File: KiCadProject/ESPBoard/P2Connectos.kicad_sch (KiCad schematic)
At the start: 0 parts

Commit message: ESP board layout mostly done. Small updates to battery management board
Signed-off-by: Eldalote.Electronics <Eldalote.Electronics@gmail.com>
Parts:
- added D201, D202, D203, D204, D205, D206, D207, D208, D209, D210, D211, D212, D213, D214, D215, D216, D217, D218, D219, D220: 3v3, Diode_SMD:D_0402_1005Metric, symbol Device:D_TVS
- added J201, J203: Conn_02x05, Connector_PinSocket_1.27mm:PinSocket_2x05_P1.27mm_Vertical_SMD, symbol Connector_Generic:Conn_02x05_Odd_Even
- added J202: Conn_01x02, Connector_PinSocket_1.27mm:PinSocket_1x02_P1.27mm_Vertical_SMD_Pin1Left, symbol Connector:Conn_01x02_Female
- added J204, J207: JST_SM04B, Connector_JST:JST_SH_SM04B-SRSS-TB_1x04-1MP_P1.00mm_Horizontal, symbol Connector:Conn_01x04_Male
- added J205: DNP, Connector_PinHeader_1.27mm:PinHeader_1x04_P1.27mm_Vertical, symbol Connector:Conn_01x04_Male
- added J206: JST_B5B_XH, Connector_JST:JST_XH_B5B-XH-A_1x05_P2.50mm_Vertical, symbol Connector:Conn_01x05_Male
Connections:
- new net +3V3: D205.2 (A2), D208.2 (A2), D217.2 (A2), D220.2 (A2), J201.1 (Pin_1), J201.2 (Pin_2), J203.1 (Pin_1), J203.2 (Pin_2), J205.1 (Pin_1), J207.1 (Pin_1)
- new net BQ_CHRG_OK: D203.2 (A2), J201.8 (Pin_8)
- new net BQ_CMPOUT: D211.2 (A2), J203.8 (Pin_8)
- new net BQ_EN_OTG: D212.2 (A2), J203.4 (Pin_4)
- new net BQ_IADPT: D210.2 (A2), J203.7 (Pin_7)
- new net BQ_IBAT: D209.2 (A2), J203.3 (Pin_3)
- new net C_USB_D+: D206.2 (A2), J202.1 (Pin_1)
- new net C_USB_D-: D207.2 (A2), J202.2 (Pin_2)
- new net Cell1: J206.4 (Pin_4)
- new net Cell2: J206.3 (Pin_3)
- new net Cell3: J206.2 (Pin_2)
- new net Cell4: J206.1 (Pin_1)
- new net GND: D201.1 (A1), D202.1 (A1), D203.1 (A1), D204.1 (A1), D205.1 (A1), D206.1 (A1), D207.1 (A1), D208.1 (A1), D209.1 (A1), D210.1 (A1), D211.1 (A1), D212.1 (A1), D213.1 (A1), D214.1 (A1), D215.1 (A1), D216.1 (A1), D217.1 (A1), D218.1 (A1), D219.1 (A1), D220.1 (A1), J201.10 (Pin_10), J201.5 (Pin_5), J201.6 (Pin_6), J201.9 (Pin_9), J203.10 (Pin_10), J203.5 (Pin_5), J203.6 (Pin_6), J203.9 (Pin_9), J204.1 (Pin_1), J204.4 (Pin_4), J205.4 (Pin_4), J206.5 (Pin_5), J207.4 (Pin_4)
- new net I2C_SCL: D204.2 (A2), D218.2 (A2), J201.4 (Pin_4), J207.3 (Pin_3)
- new net I2C_SDA: D201.2 (A2), D219.2 (A2), J201.3 (Pin_3), J207.2 (Pin_2)
- new net MAINLED_PWM: D213.2 (A2), J204.3 (Pin_3)
- new net MAINLED_nFTL: D214.2 (A2), J204.2 (Pin_2)
- new net UART_RXDO: D216.2 (A2), J205.2 (Pin_2)
- new net UART_TXDO: D215.2 (A2), J205.3 (Pin_3)
- new net USBPD_INT_N: D202.2 (A2), J201.7 (Pin_7)
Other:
- note added: "Back up programming pins"
- note added: "Battery Balancing port"
- note added: "Board to board "home made mezzanine" connection to Battery management PCB"
- note added: "Direct lines to LED driver board"
- note added: "I2C connector to hall board, daisy over to led driver board from there"

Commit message: Tweaking
Signed-off-by: Eldalote.Electronics <Eldalote.Electronics@gmail.com>
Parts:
- removed D201, D202, D203, D204, D205, D206, D207, D208, D209, D210, D211, D212, D213, D214, D215, D216, D217, D218, D219, D220: 3v3, Diode_SMD:D_0402_1005Metric, symbol Device:D_TVS
- J205: footprint Connector_PinHeader_1.27mm:PinHeader_1x04_P1.27mm_Vertical -> Connector_PinHeader_1.27mm:PinHeader_2x02_P1.27mm_Vertical_SMD
- J206: value JST_B5B_XH -> 1x05 female; footprint Connector_JST:JST_XH_B5B-XH-A_1x05_P2.50mm_Vertical -> Connector_PinSocket_1.27mm:PinSocket_1x05_P1.27mm_Vertical_SMD_Pin1Left; symbol Connector:Conn_01x05_Male -> Connector:Conn_01x05_Female

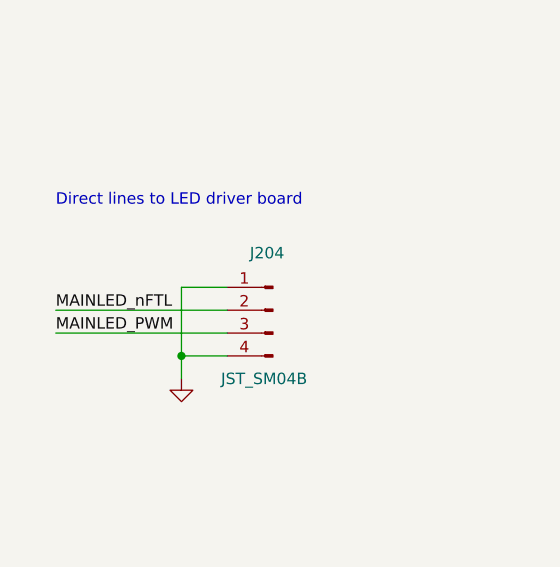
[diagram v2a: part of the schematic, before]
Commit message: Final touches before component order and PCB layout
Signed-off-by: Eldalote.Electronics <Eldalote.Electronics@gmail.com>
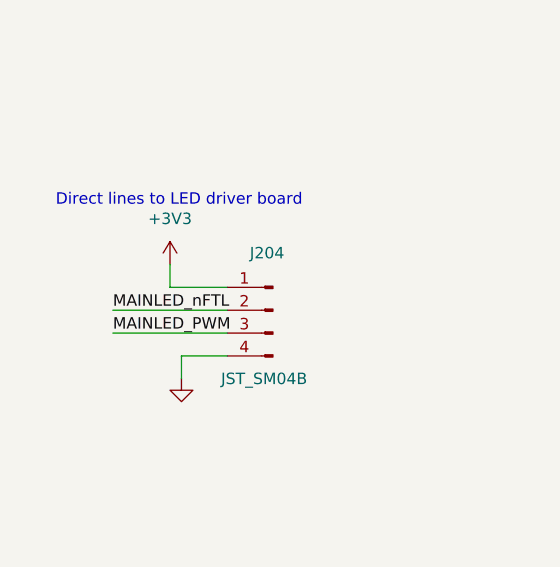
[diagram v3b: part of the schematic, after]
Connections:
- net +3V3: now also J204.1 (Pin_1)
- net GND: no longer J204.1 (Pin_1)
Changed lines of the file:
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@@
   (junction (at 95.25 69.85) (diameter 0) (color 0 0 0 0)
   )
-  (junction (at 36.83 154.94) (diameter 0) (color 0 0 0 0)
-  )
   (wire (pts (xy 142.24 171.45) (xy 154.94 171.45))
     (stroke (width 0) (type default) (color 0 0 0 0))
@@
     (stroke (width 0) (type default) (color 0 0 0 0))
   )
-  (wire (pts (xy 22.86 149.86) (xy 41.91 149.86))
+  (wire (pts (xy 29.21 149.86) (xy 41.91 149.86))
     (stroke (width 0) (type default) (color 0 0 0 0))
   )
@@
     (stroke (width 0) (type default) (color 0 0 0 0))
   )
-  (wire (pts (xy 36.83 147.32) (xy 36.83 154.94))
-    (stroke (width 0) (type default) (color 0 0 0 0))
-  )
   (wire (pts (xy 34.29 43.18) (xy 46.99 43.18))
     (stroke (width 0) (type default) (color 0 0 0 0))
@@
     (stroke (width 0) (type default) (color 0 0 0 0))
   )
-  (wire (pts (xy 41.91 147.32) (xy 36.83 147.32))
+  (wire (pts (xy 35.56 147.32) (xy 41.91 147.32))
     (stroke (width 0) (type default) (color 0 0 0 0))
   )
@@
     (stroke (width 0) (type default) (color 0 0 0 0))
   )
-  (wire (pts (xy 22.86 152.4) (xy 41.91 152.4))
+  (wire (pts (xy 29.21 152.4) (xy 41.91 152.4))
+    (stroke (width 0) (type default) (color 0 0 0 0))
+  )
+  (wire (pts (xy 35.56 147.32) (xy 35.56 144.78))
     (stroke (width 0) (type default) (color 0 0 0 0))
   )
@@
     (effects (font (size 1.27 1.27)) (justify left bottom))
   )
-  (label "MAINLED_PWM" (at 22.86 152.4 0)
+  (label "MAINLED_PWM" (at 29.21 152.4 0)
     (effects (font (size 1.27 1.27)) (justify left bottom))
   )
@@
     (effects (font (size 1.27 1.27)) (justify right bottom))
   )
-  (label "MAINLED_nFTL" (at 22.86 149.86 0)
+  (label "MAINLED_nFTL" (at 29.21 149.86 0)
     (effects (font (size 1.27 1.27)) (justify left bottom))
   )
@@
       (effects (font (size 1.27 1.27)) hide)
     )
+    (pin "1")
+  )
+  (symbol (lib_id "power:+3V3") (at 35.56 144.78 0) (unit 1)
+    (in_bom yes) (on_board yes)
+    (property "Reference" "#PWR?" (id 0) (at 35.56 148.59 0)
+      (effects (font (size 1.27 1.27)) hide)
+    )
+    (property "Value" "+3V3" (id 1) (at 35.56 139.7 0))
+    (property "Footprint" "" (id 2) (at 35.56 144.78 0)
+      (effects (font (size 1.27 1.27)) hide)
+    )
+    (property "Datasheet" "" (id 3) (at 35.56 144.78 0)
+      (effects (font (size 1.27 1.27)) hide)
+    )

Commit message: Components selected, MfID added to schematics, and components ordered
Signed-off-by: Eldalote.Electronics <Eldalote.Electronics@gmail.com>
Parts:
- J201, J203: MfID (none) -> 20021321-00010C4LF
- J202: MfID (none) -> M50-3140245
- J204, J207: MfID (none) -> SM04B-SRSS-TB(LF)(SN)
- J205: MfID (none) -> GRPB022VWQS-RC
- J206: MfID (none) -> M50-3140545
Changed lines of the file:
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@@
+      (effects (font (size 1.27 1.27)) hide)
+    )
+    (property "MfID" "M50-3140545" (id 4) (at 245.11 129.54 0)
       (effects (font (size 1.27 1.27)) hide)
     )
@@
   (symbol (lib_id "power:+3V3") (at 35.56 144.78 0) (unit 1)
     (in_bom yes) (on_board yes)
-    (property "Reference" "#PWR?" (id 0) (at 35.56 148.59 0)
+    (property "Reference" "#PWR0110" (id 0) (at 35.56 148.59 0)
       (effects (font (size 1.27 1.27)) hide)
     )
@@
       (effects (font (size 1.27 1.27)) hide)
     )
+    (property "MfID" "M50-3140245" (id 4) (at 255.27 46.99 0)
+      (effects (font (size 1.27 1.27)) hide)
+    )
     (pin "1")
     (pin "2")
@@
       (effects (font (size 1.27 1.27)) hide)
     )
+    (property "MfID" "GRPB022VWQS-RC" (id 4) (at 160.02 168.91 0)
+      (effects (font (size 1.27 1.27)) hide)
+    )
     (pin "1")
     (pin "2")
@@
       (effects (font (size 1.27 1.27)) hide)
     )
+    (property "MfID" "SM04B-SRSS-TB(LF)(SN)" (id 4) (at 125.73 110.49 0)
+      (effects (font (size 1.27 1.27)) hide)
+    )
     (pin "1")
     (pin "2")
@@
     )
     (property "Datasheet" "~" (id 3) (at 46.99 149.86 0)
+      (effects (font (size 1.27 1.27)) hide)
+    )
+    (property "MfID" "SM04B-SRSS-TB(LF)(SN)" (id 4) (at 46.99 149.86 0)
       (effects (font (size 1.27 1.27)) hide)
     )
@@
     )
     (property "Datasheet" "~" (id 3) (at 109.22 53.34 0)
+      (effects (font (size 1.27 1.27)) hide)
+    )
+    (property "MfID" "20021321-00010C4LF" (id 4) (at 109.22 53.34 0)
       (effects (font (size 1.27 1.27)) hide)
     )
@@
       (effects (font (size 1.27 1.27)) hide)
     )
+    (property "MfID" "20021321-00010C4LF" (id 4) (at 184.15 54.61 0)
+      (effects (font (size 1.27 1.27)) hide)
+    )

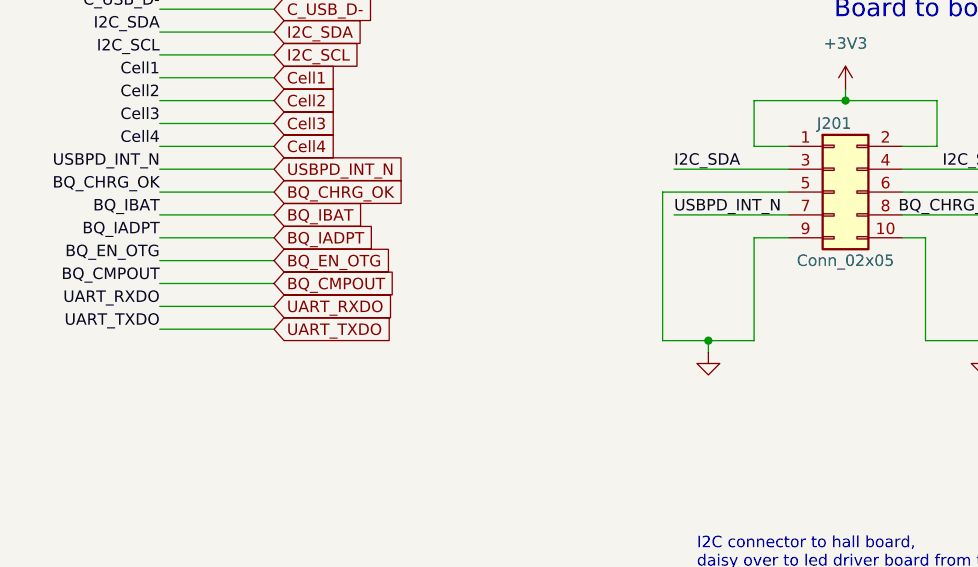
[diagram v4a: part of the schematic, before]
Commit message: Finished v0.1 of BatMan PCB, started layout of ESP PCB
Signed-off-by: Eldalote.Electronics <Eldalote.Electronics@gmail.com>
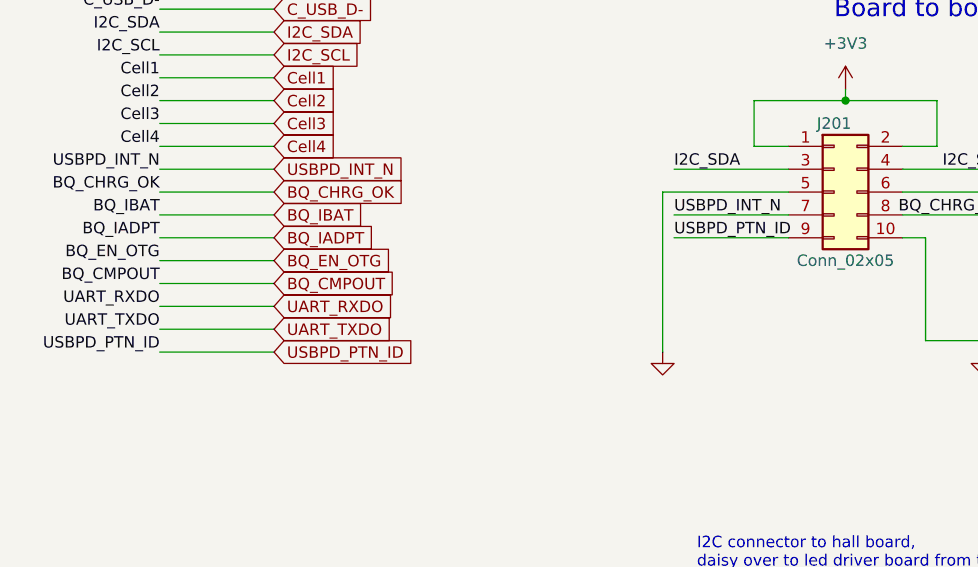
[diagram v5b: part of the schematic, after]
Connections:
- net GND: no longer J201.9 (Pin_9)
- new net USBPD_PTN_ID: J201.9 (Pin_9)
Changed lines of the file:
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@@
   (junction (at 172.72 68.58) (diameter 0) (color 0 0 0 0)
   )
-  (junction (at 95.25 69.85) (diameter 0) (color 0 0 0 0)
-  )
   (wire (pts (xy 142.24 171.45) (xy 154.94 171.45))
     (stroke (width 0) (type default) (color 0 0 0 0))
@@
     (stroke (width 0) (type default) (color 0 0 0 0))
   )
-  (wire (pts (xy 90.17 53.34) (xy 90.17 69.85))
+  (wire (pts (xy 90.17 53.34) (xy 90.17 71.12))
     (stroke (width 0) (type default) (color 0 0 0 0))
   )
@@
     (stroke (width 0) (type default) (color 0 0 0 0))
   )
-  (wire (pts (xy 95.25 69.85) (xy 100.33 69.85))
-    (stroke (width 0) (type default) (color 0 0 0 0))
-  )
   (wire (pts (xy 34.29 60.96) (xy 46.99 60.96))
     (stroke (width 0) (type default) (color 0 0 0 0))
@@
     (stroke (width 0) (type default) (color 0 0 0 0))
   )
+  (wire (pts (xy 91.44 58.42) (xy 104.14 58.42))
+    (stroke (width 0) (type default) (color 0 0 0 0))
+  )
   (wire (pts (xy 185.42 43.18) (xy 185.42 44.45))
     (stroke (width 0) (type default) (color 0 0 0 0))
   )
+  (wire (pts (xy 34.29 71.12) (xy 46.99 71.12))
+    (stroke (width 0) (type default) (color 0 0 0 0))
+  )
   (wire (pts (xy 234.95 134.62) (xy 234.95 137.16))
     (stroke (width 0) (type default) (color 0 0 0 0))
@@
     (stroke (width 0) (type default) (color 0 0 0 0))
   )
-  (wire (pts (xy 95.25 71.12) (xy 95.25 69.85))
-    (stroke (width 0) (type default) (color 0 0 0 0))
-  )
   (wire (pts (xy 195.58 44.45) (xy 195.58 49.53))
     (stroke (width 0) (type default) (color 0 0 0 0))
   )
-  (wire (pts (xy 100.33 58.42) (xy 100.33 69.85))
-    (stroke (width 0) (type default) (color 0 0 0 0))
-  )
   (wire (pts (xy 205.74 54.61) (xy 191.77 54.61))
     (stroke (width 0) (type default) (color 0 0 0 0))
@@
     (stroke (width 0) (type default) (color 0 0 0 0))
   )
-  (wire (pts (xy 90.17 69.85) (xy 95.25 69.85))
-    (stroke (width 0) (type default) (color 0 0 0 0))
-  )
   (wire (pts (xy 34.29 50.8) (xy 46.99 50.8))
     (stroke (width 0) (type default) (color 0 0 0 0))
@@
   )
   (wire (pts (xy 172.72 68.58) (xy 167.64 68.58))
-    (stroke (width 0) (type default) (color 0 0 0 0))
-  )
-  (wire (pts (xy 100.33 58.42) (xy 104.14 58.42))
     (stroke (width 0) (type default) (color 0 0 0 0))
   )
@@
     (effects (font (size 1.27 1.27)) (justify right bottom))
   )
+  (label "USBPD_PTN_ID" (at 34.29 71.12 180)
+    (effects (font (size 1.27 1.27)) (justify right bottom))
+  )
   (label "C_USB_D+" (at 233.68 46.99 0)
     (effects (font (size 1.27 1.27)) (justify left bottom))
@@
     (effects (font (size 1.27 1.27)) (justify left bottom))
   )
+  (label "USBPD_PTN_ID" (at 91.44 58.42 0)
+    (effects (font (size 1.27 1.27)) (justify left bottom))
+  )
   (label "BQ_IBAT" (at 171.45 52.07 0)
     (effects (font (size 1.27 1.27)) (justify left bottom))
@@
     (effects (font (size 1.27 1.27)) (justify left))
     (property "Intersheet References" "${INTERSHEET_REFS}" (id 0) (at 59.2607 30.4006 0)
+      (effects (font (size 1.27 1.27)) (justify left) hide)
+    )
+  )
+  (global_label "USBPD_PTN_ID" (shape input) (at 46.99 71.12 0) (fields_autoplaced)
+    (effects (font (size 1.27 1.27)) (justify left))
+    (property "Intersheet References" "${INTERSHEET_REFS}" (id 0) (at 63.1312 71.0406 0)
       (effects (font (size 1.27 1.27)) (justify left) hide)
     )
@@
     (pin "4")
   )
-  (symbol (lib_id "power:GND") (at 95.25 71.12 0) (unit 1)
+  (symbol (lib_id "power:GND") (at 90.17 71.12 0) (unit 1)
     (in_bom yes) (on_board yes) (fields_autoplaced)
-    (property "Reference" "#PWR0201" (id 0) (at 95.25 77.47 0)
-      (effects (font (size 1.27 1.27)) hide)
-    )
-    (property "Value" "GND" (id 1) (at 95.25 76.2 0)
-      (effects (font (size 1.27 1.27)) hide)
-    )
-    (property "Footprint" "" (id 2) (at 95.25 71.12 0)
-      (effects (font (size 1.27 1.27)) hide)
-    )
-    (property "Datasheet" "" (id 3) (at 95.25 71.12 0)
-      (effects (font (size 1.27 1.27)) hide)
-    )
+    (property "Reference" "#PWR0201" (id 0) (at 90.17 77.47 0)
+      (effects (font (size 1.27 1.27)) hide)
+    )
+    (property "Value" "GND" (id 1) (at 90.17 76.2 0)
+      (effects (font (size 1.27 1.27)) hide)
+    )
+    (property "Footprint" "" (id 2) (at 90.17 71.12 0)
+      (effects (font (size 1.27 1.27)) hide)
+    )
+    (property "Datasheet" "" (id 3) (at 90.17 71.12 0)
+      (effects (font (size 1.27 1.27)) hide)
+    )
